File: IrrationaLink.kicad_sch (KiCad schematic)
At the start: 37 parts, among them J1 USB_C_Receptacle_USB2.0, J2 Conn_02x05_Odd_Even, J3 Conn_02x05_Odd_Even, SW1 SW_Push, U1 ESP32-C3, U2 LM2937xMP, Y1 ABM11W-32.0000MHZ-7-D1X-T3

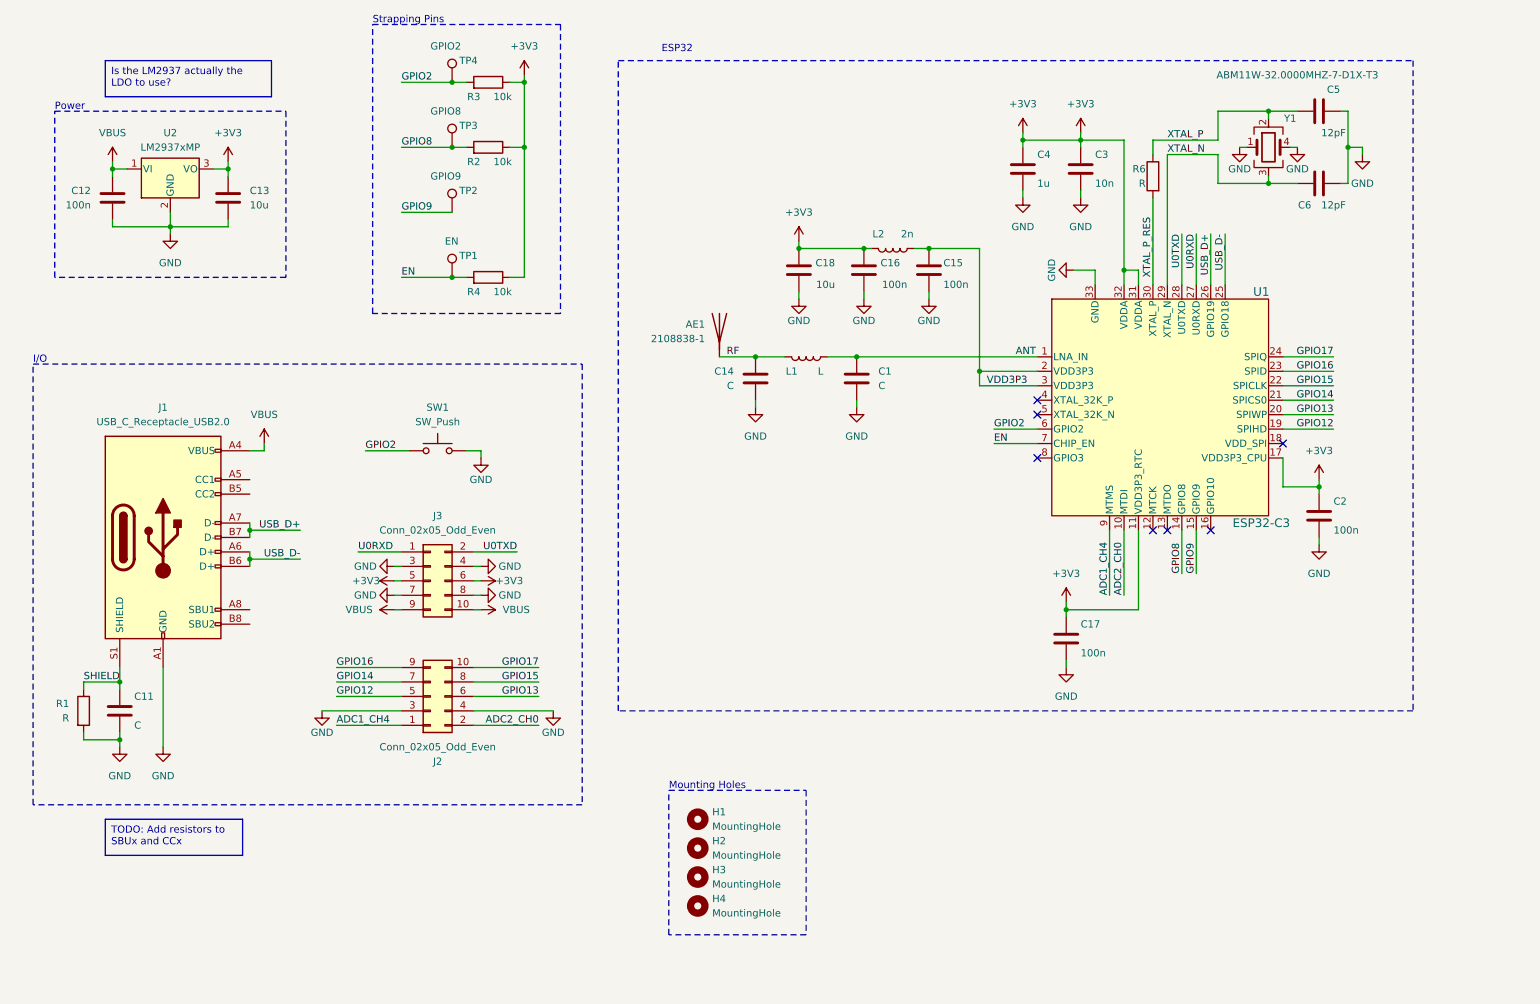
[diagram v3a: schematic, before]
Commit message: Connect Crystal; Add 500R resistor to U0TXD
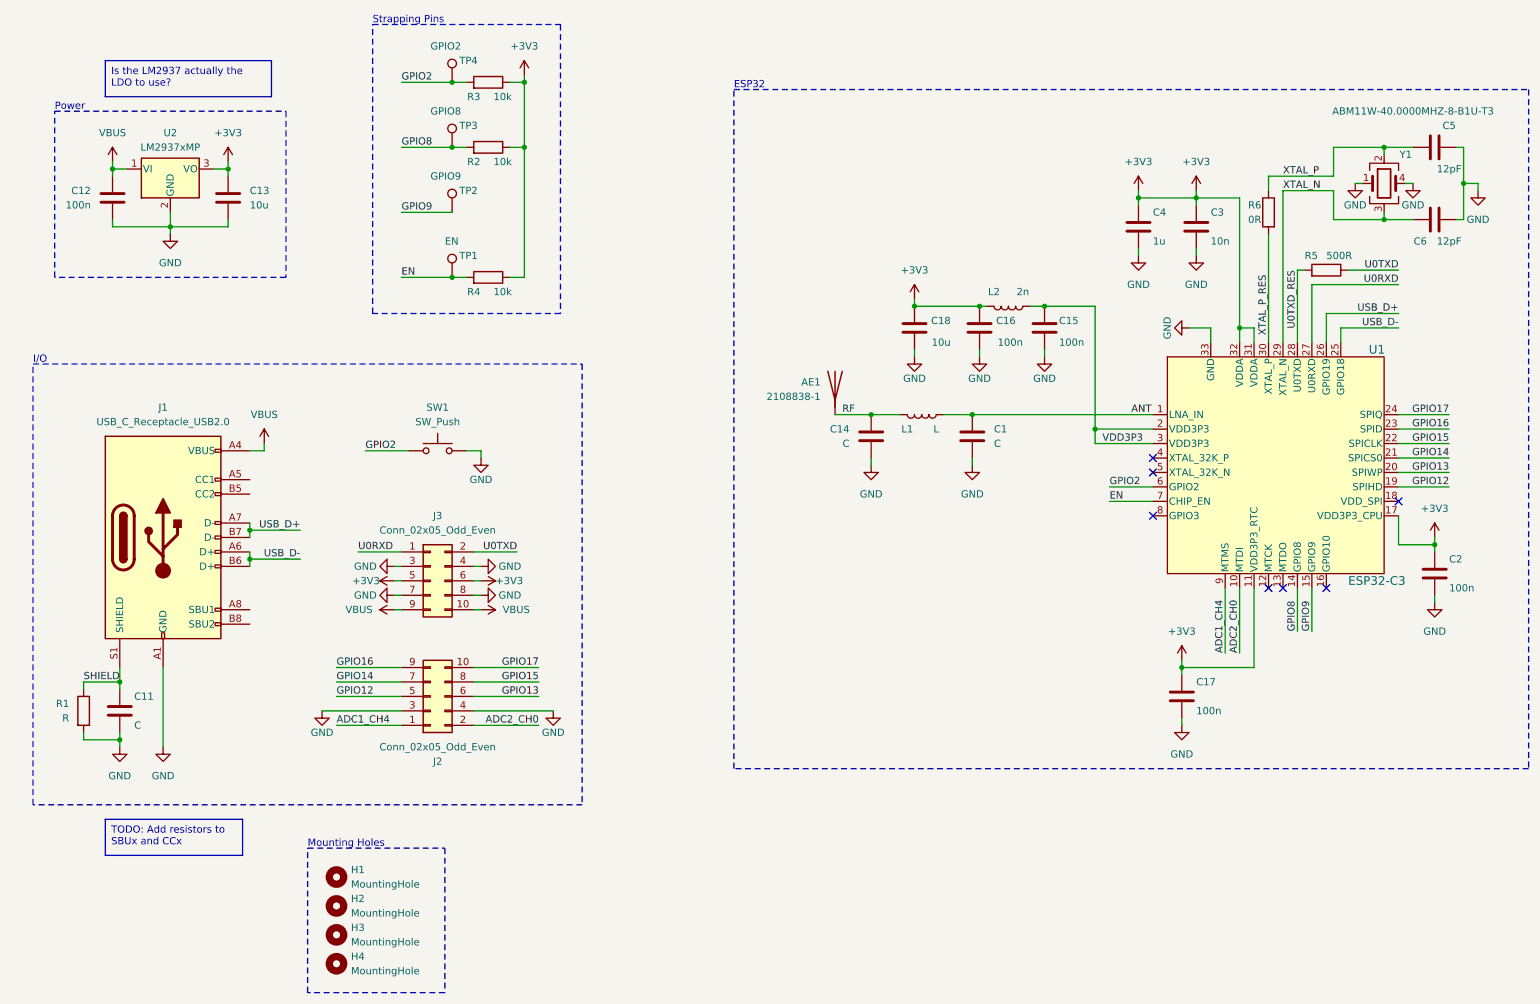
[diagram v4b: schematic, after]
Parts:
- added R5: 500R, Resistor_SMD:R_0402_1005Metric, symbol Device:R
- C11: footprint Capacitor_SMD:C_0603_1608Metric -> Capacitor_SMD:C_0402_1005Metric
- R6: value R -> 0R
- Y1: value ABM11W-32.0000MHZ-7-D1X-T3 -> ABM11W-40.0000MHZ-8-B1U-T3
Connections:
- net U0TXD: now also R5.1; no longer U1.28 (U0TXD)
- new net U0TXD_RES: R5.2, U1.28 (U0TXD)
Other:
- moved on the sheet: AE1, C1, C14, C15, C16, C17, C18, C2, C3, C4, C5, C6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

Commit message: Add USB pullups/downs and clean up schematic
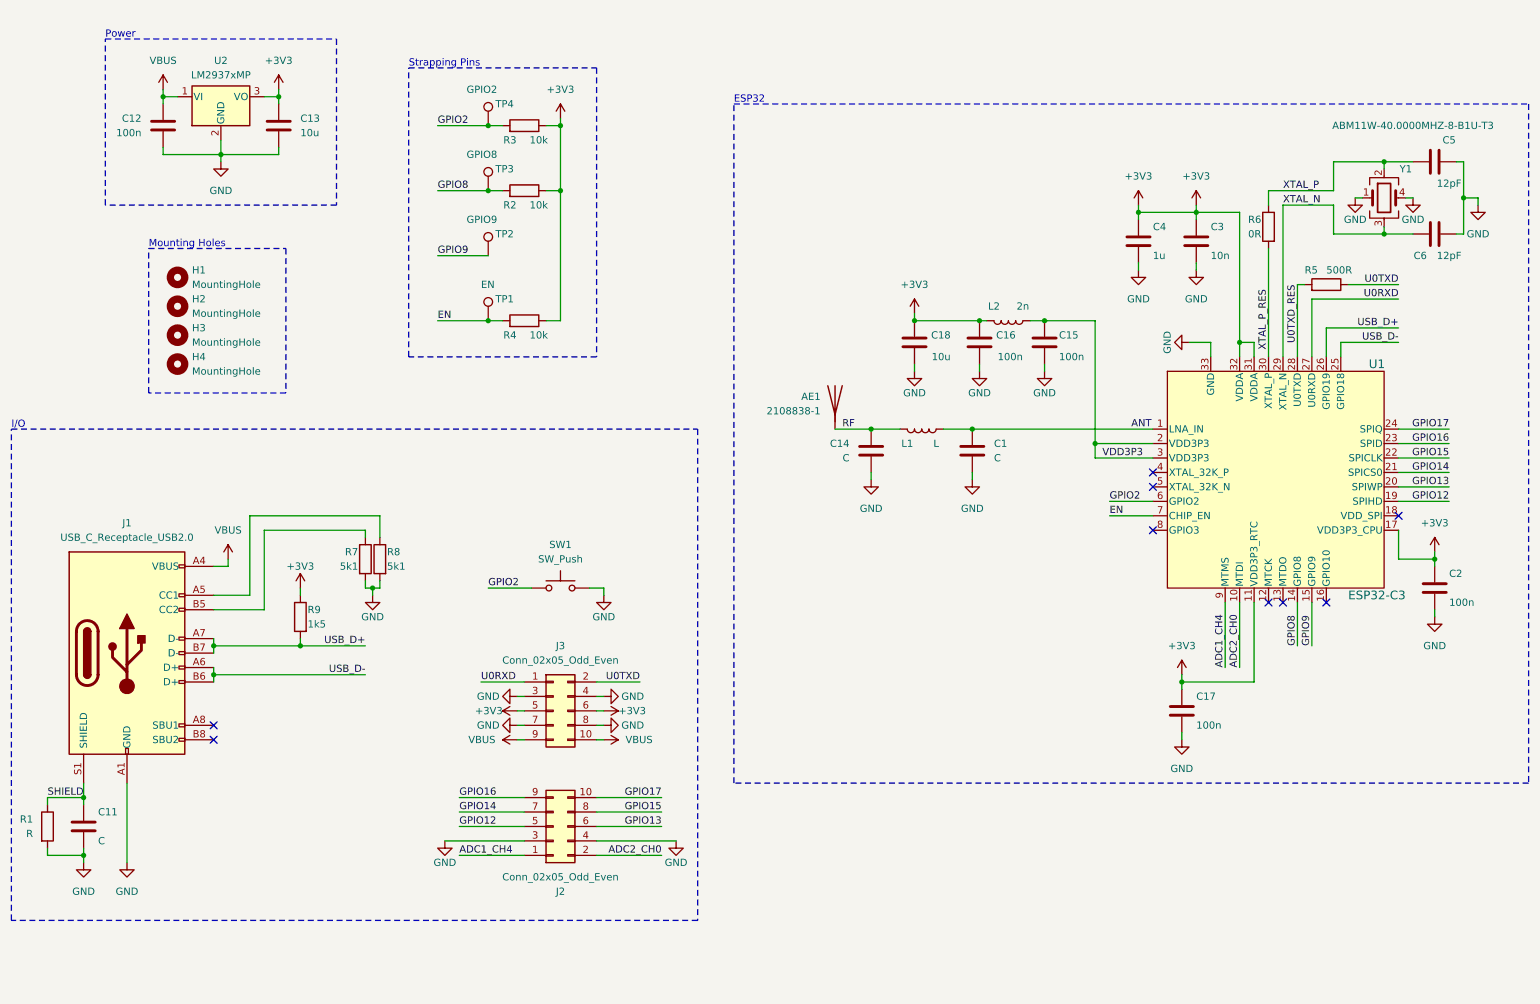
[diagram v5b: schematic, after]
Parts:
- added R7, R8: 5k1, Resistor_SMD:R_0402_1005Metric, symbol Device:R
- added R9: 1k5, Resistor_SMD:R_0402_1005Metric, symbol Device:R
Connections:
- net +3V3: now also R9.1
- net GND: now also R7.2, R8.2
- net USB_D+: now also R9.2
- net at J1.A5 (CC1): now also R8.1
- net at J1.B5 (CC2): now also R7.1
- no-connect marks 7 -> 9
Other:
- moved on the sheet: AE1, C1, C11, C12, C13, C14, C15, C16, C17, C18, C2, C3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

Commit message: Add USB resistors to PCB
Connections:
- net CC1: now reaches J1.A5 (CC1), R8.1
- net CC2: now reaches J1.B5 (CC2), R7.1
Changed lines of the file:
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@@
+    (effects (font (size 1.27 1.27)) (justify left bottom))
+  )
+  (label "CC1" (at 50.8 124.46 0) (fields_autoplaced)
     (effects (font (size 1.27 1.27)) (justify left bottom))
   )
@@
     (effects (font (size 1.27 1.27)) (justify right bottom))
   )
+  (label "CC2" (at 50.8 127 0) (fields_autoplaced)
+    (effects (font (size 1.27 1.27)) (justify left bottom))
+  )
   (label "GPIO15" (at 266.7 100.33 180) (fields_autoplaced)
